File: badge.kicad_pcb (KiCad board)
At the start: 2 copper layers, 68.6 x 129.5 mm, 38 parts, among them J1 DevKitC_L, J10 IR333C, J11 DUST, J12 DevKitC_L_SMD, J13 DevKitC_R_SMD, J14 220uF, J2 DevKitC_R, J4 ADC_3, J5 ADC_2, J6 ADC_1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

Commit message: Change button
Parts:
- removed the J6 at (166.4, 116.8) (x3)
- removed the SW6 at (149.9, 109.2)
- added J6 (x3): ADC_1, custom_footprint:PinSocket_1x04_P2.54mm_Vertical_NO3D_2S, F.Cu at (166.4, 116.8)
- added SW6: B, Button_Switch_SMD:SW_SPST_PTS645, F.Cu at (152.4, 111.8)
- added SW6: B, Button_Switch_SMD:SW_SPST_PTS810, F.Cu at (149.9, 109.2)
- SW3: footprint Button_Switch_SMD:SW_SPST_TL3342 -> Button_Switch_SMD:SW_SPST_PTS645
- moved SW7 3.59 mm to (121.9, 114.3)
- moved SW3 2.54 mm to (144.8, 119.4)

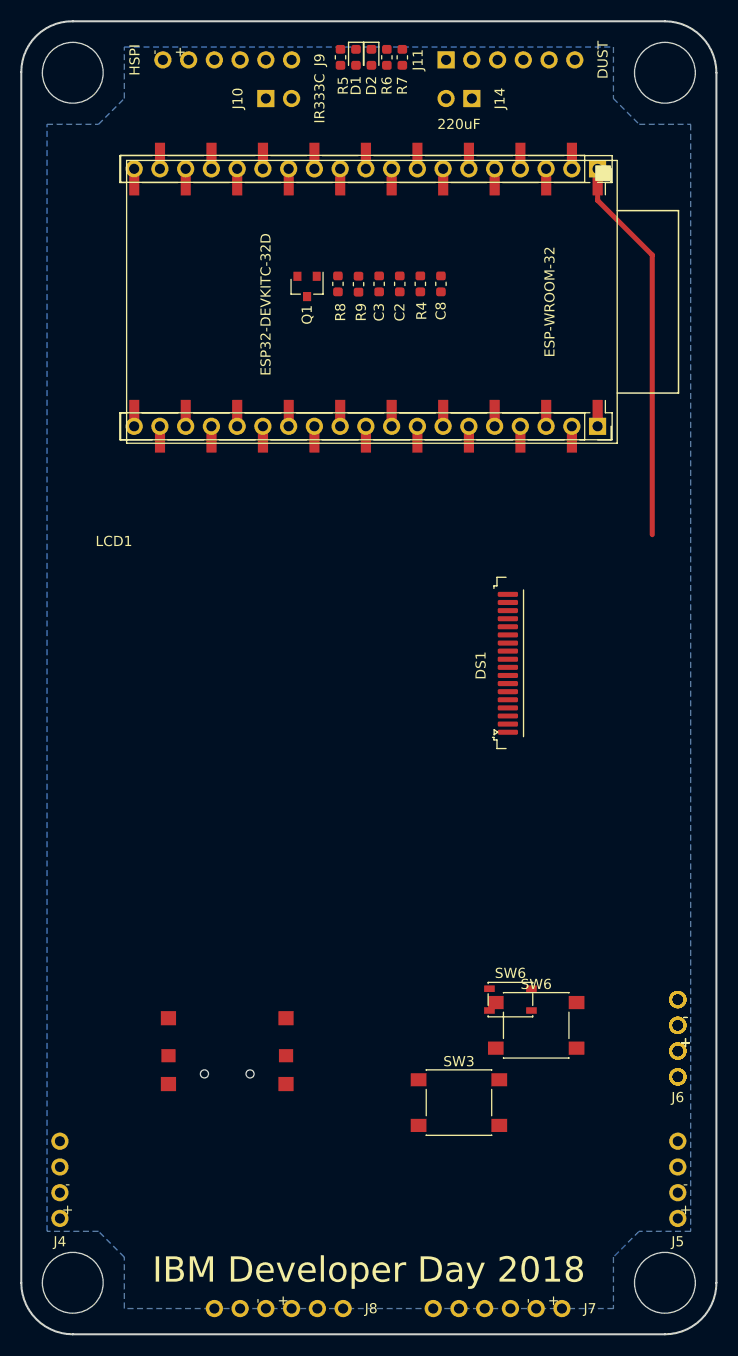
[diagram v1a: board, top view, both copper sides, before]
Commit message: Update v0.4, vertical long before tracks
* Move footprint library to DeveloperDay2018Badge
* Add symbol library, 3D models into project
* Change board color
* Increase R, C, LED size to 0805(2012)
* Remove front solder mask for ESP32 DevKitC socket header, to make clean SMD socket pad.
* Add silk for ESP32 DevKitC
* Add silk direction in footprint for ITS-1550S-B 5 way tact switch
* Add footprint and 3D for ITS-1106 tact switch
* Change ESP32 DevKitC 3D model from SnapEDA
* Remove THT 19pin socket 3D for ESP32 DevKitC
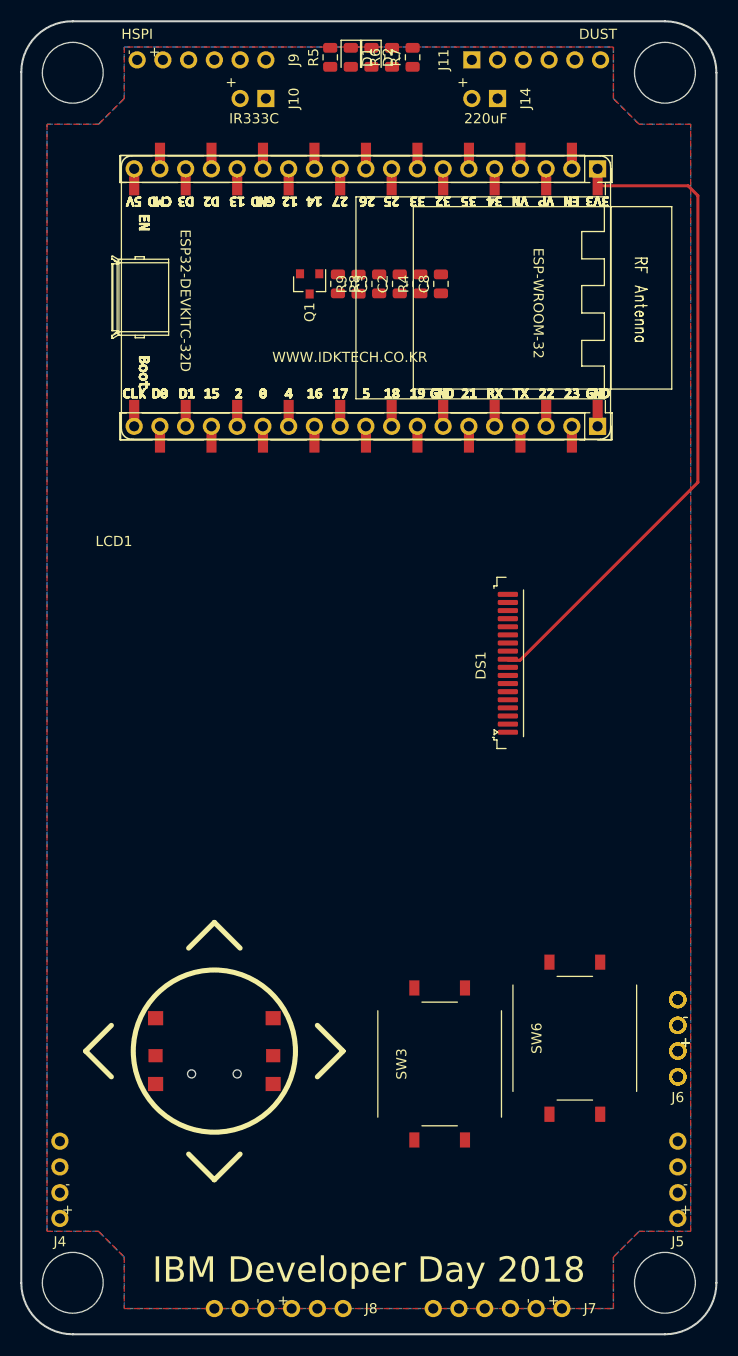
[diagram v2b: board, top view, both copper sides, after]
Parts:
- removed the J6 at (166.4, 116.8) (x3)
- removed the SW6 at (152.4, 111.8)
- removed the SW6 at (149.9, 109.2)
- added J6 (x3): ADC_1, custom_footprint:PinSocket_1x04_P2.54mm_Vertical_NO3D_2S, F.Cu at (166.4, 116.8)
- added SW6: B, DeveloperDay2018Badge:ITS-1106S, F.Cu at (156.2, 113.0)
- C2, C3: value 0603/0.1uF -> 2012/0.1uF; footprint Capacitor_SMD:C_0603_1608Metric -> Capacitor_SMD:C_0805_2012Metric
- C8: value 0.1uF -> 2012/0.1uF; footprint Capacitor_SMD:C_0603_1608Metric -> Capacitor_SMD:C_0805_2012Metric
- D1: value 0603/BLUE -> 2012/BLUE; footprint LED_SMD:LED_0603_1608Metric -> LED_SMD:LED_0805_2012Metric
- D2: value 0603/RED -> 2012/RED; footprint LED_SMD:LED_0603_1608Metric -> LED_SMD:LED_0805_2012Metric
- J1, J2: footprint Connector_PinSocket_2.54mm:PinSocket_1x19_P2.54mm_Vertical -> DeveloperDay2018Badge:PinSocket_1x19_P2.54mm_Vertical_BackOnly_NO3D
- J10, J14: footprint custom_footprint:PinSocket_1x02_P2.54mm_Vertical_NO3D -> DeveloperDay2018Badge:PinSocket_1x02_P2.54mm_Vertical_NO3D
- LCD1: footprint custom_footprint:2.4INCH_TFT_LCD_18P_0.80mm_FOLD -> DeveloperDay2018Badge:2.4INCH_TFT_LCD_18P_0.80mm_FOLD_JGKONG
- R4: value 0603/4.7R -> 2012/4.7R; footprint Resistor_SMD:R_0603_1608Metric -> Resistor_SMD:R_0805_2012Metric
- R5: value 0603/470R -> 2012/470R; footprint Resistor_SMD:R_0603_1608Metric -> Resistor_SMD:R_0805_2012Metric
- R6: value 0603/1K -> 2012/1K; footprint Resistor_SMD:R_0603_1608Metric -> Resistor_SMD:R_0805_2012Metric
- R7: value 0603/220R -> 2012/220R; footprint Resistor_SMD:R_0603_1608Metric -> Resistor_SMD:R_0805_2012Metric
- R8: value 0603/20R -> 2012/20R; footprint Resistor_SMD:R_0603_1608Metric -> Resistor_SMD:R_0805_2012Metric
- R9: value 0603/36R -> 2012/36R; footprint Resistor_SMD:R_0603_1608Metric -> Resistor_SMD:R_0805_2012Metric
- SW3: footprint Button_Switch_SMD:SW_SPST_PTS645 -> DeveloperDay2018Badge:ITS-1106S
- SW7: value SW_DIP_x03 -> ITS_1500S_B; footprint custom_footprint:ITS-1500S-A -> DeveloperDay2018Badge:ITS-1500S-B-SILKDIR
- U1: footprint custom_footprint:MODULE_ESP32-DEVKITC-32D-SILKONLY -> DeveloperDay2018Badge:MODULE_ESP32-DEVKITC-32D-SILKONLY-SIMPLE
- moved SW3 4.26 mm to (142.9, 115.6), turned to 90 degrees
- moved J11 2.54 mm to (146.1, 16.5)
- moved J9 2.54 mm to (125.7, 16.5)
- moved J14 2.54 mm to (148.6, 20.3)
- moved SW7 1.27 mm to (120.7, 114.3)
- moved R5 1.02 mm to (132.1, 16.3)
- moved R7 1.02 mm to (140.2, 16.3)
- moved U1 0.65 mm to (138.7, 40.0)
- moved D1 0.51 mm to (134.1, 16.3)
- moved R6 0.51 mm to (138.2, 16.3)
- moved Q1 0.36 mm to (130.0, 38.6)
- turned J10 to 270 degrees
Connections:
- J10 pad 2: +3V3 -> +5V
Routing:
- net +3V3: track 38.3 -> 66.3 mm
- added copper zone on F.Cu, net GND
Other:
- net class Default: trace_width 0.5 -> 0.3
- board text added: "WWW.IDKTECH.CO.KR"

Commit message: Rout'ing
* Add dummy pad for ESP32 DevKitC footprint to avoid errors
* Add silk guide for LCD attachment
* Add alternative 40pin LCD connector
* Add logo and information in silk layer
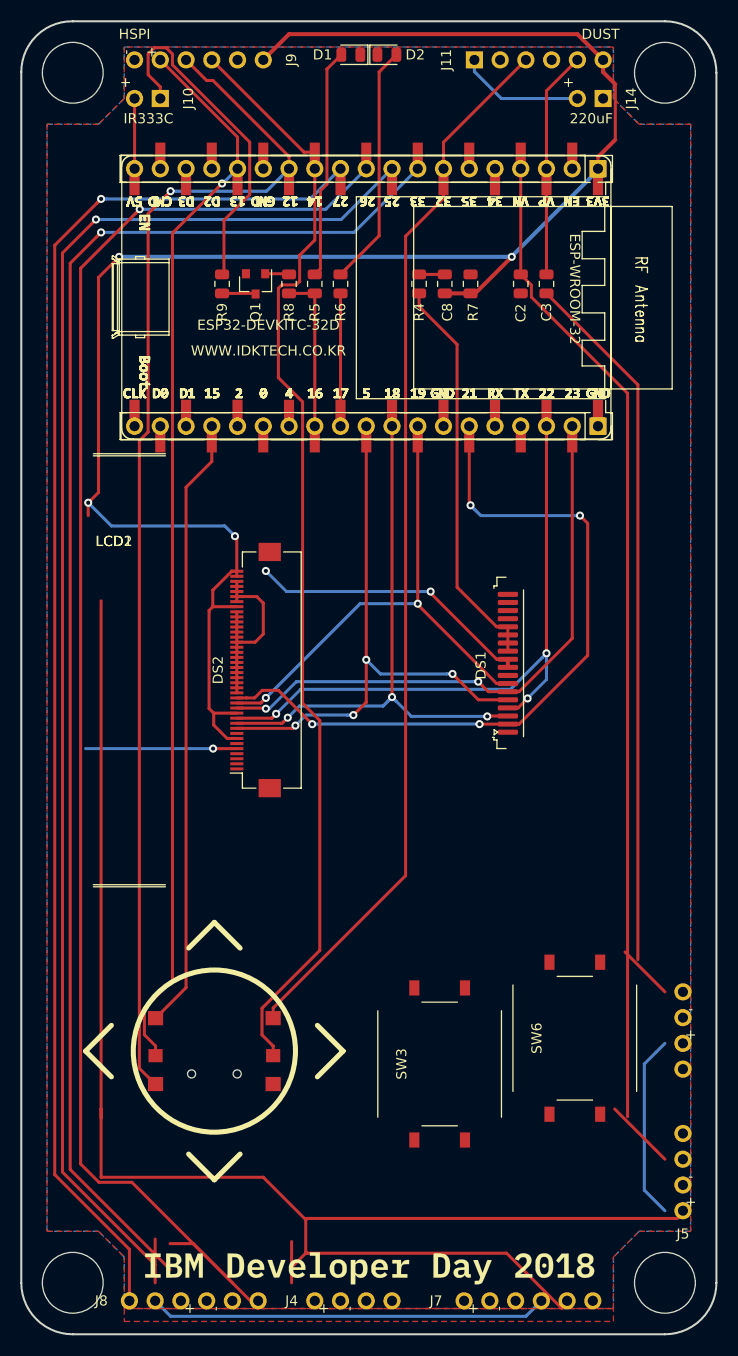
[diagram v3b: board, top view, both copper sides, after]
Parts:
- removed the J6 at (166.4, 116.8) (x4)
- added DS2: 40PIN LCD, Connector_FFC-FPC:Hirose_FH12-40S-0.5SH_1x40-1MP_P0.50mm_Horizontal, F.Cu at (124.7, 76.7)
- added G***: LOGO, LOGO, B.Cu at (121.9, 129.5)
- added G***: LOGO, LOGO, B.Cu at (135.9, 114.3)
- added G***: Badge URL, LOGO, B.Cu at (143.5, 62.2)
- added G***: LOGO_INFO, LOGO, B.Cu at (142.2, 95.2)
- added G***: Front Logo, DeveloperDay2018Badge:LOGO_Front, F.Cu at (136.4, 135.6)
- added G***: LOGO, LOGO, B.Cu at (149.9, 77.5)
- added J6: ADC_1, custom_footprint:PinSocket_1x04_P2.54mm_Vertical_NO3D_2S, F.Cu at (166.9, 116.1)
- added LCD2: 2.4" LCD 40PIN, DeveloperDay2018Badge:2.4INCH_TFT_LCD_40P_0.50mm_FOLD, F.Cu at (105.7, 55.4)
- DS1: value EZ240IT010 -> 18PIN LCD
- LCD1: value 2.4" LCD -> 2.4" LCD 18PIN
- moved J4 26.4 mm to (130.6, 138.9), turned to 90 degrees
- moved R7 23.1 mm to (145.9, 38.6), turned to 270 degrees
- moved R6 22.9 mm to (133.1, 38.6), turned to 270 degrees
- moved R5 22.4 mm to (130.6, 38.6), turned to 270 degrees
- moved J8 21.1 mm to (112.3, 138.9), turned to 90 degrees
- moved C3 16.5 mm to (153.4, 38.6)
- moved R9 13.5 mm to (121.4, 38.6)
- moved C2 11.9 mm to (150.9, 38.6)
- moved J10 10.4 mm to (115.3, 20.3)
- moved J14 10.4 mm to (159.0, 20.3)
- moved J7 9.68 mm to (145.3, 138.9), turned to 90 degrees
- moved Q1 5.33 mm to (124.7, 38.6)
- moved R8 4.83 mm to (128.0, 38.6)
- moved D2 1.55 mm to (137.7, 16.0), turned to 0 degrees
- moved J5 0.92 mm to (166.9, 130.0)
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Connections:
- C2 pad 2: /GPIO36 -> /GPIO39
- C3 pad 2: /GPIO39 -> /GPIO36
- D1 pad 1: Net-(D1-Pad1) -> GND
- D1 pad 2: /GPIO16 -> Net-(D1-Pad2)
- D2 pad 1: Net-(D2-Pad1) -> GND
- D2 pad 2: /GPIO17 -> Net-(D2-Pad2)
- J5 pad 3: /GPIO36 -> /GPIO39
- J5 pad 4: /GPIO39 -> /GPIO36
- R5 pad 1: GND -> Net-(D1-Pad2)
- R5 pad 2: Net-(D1-Pad1) -> /GPIO16
- R6 pad 1: GND -> Net-(D2-Pad2)
- R6 pad 2: Net-(D2-Pad1) -> /GPIO17
- R8 pad 2: /GPIO27 -> /GPIO16
- SW7 pad 1: /GPIO12 -> /GPIO15
- SW7 pad 3: /GPIO14 -> /GPIO12
- SW7 pad 5: /GPIO15 -> /GPIO14
- SW7 pad 6: /GPIO39 -> /GPIO32
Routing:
- net /GPIO33: track 1.63 -> 296.5 mm, vias 0 -> 1
- net /GPIO25: track 1.68 -> 184.9 mm, vias 0 -> 1
- net +3V3: track 66.3 -> 224.2 mm, vias 0 -> 6
- net /GPIO26: track 1.63 -> 153.4 mm, vias 0 -> 1
- net /GPIO27: track 1.68 -> 140.9 mm, vias 0 -> 1
- net /GPIO12: track 1.68 -> 119.6 mm, vias 0 -> 1
- net /GPIO14: track 1.63 -> 109.9 mm
- net /GPIO13: track 1.68 -> 107.4 mm, vias 0 -> 1
- net /GPIO39: track 1.63 -> 106.5 mm
- net /GPIO32: track 1.68 -> 103.2 mm
- net Net-(C3-Pad1): track 0.00 -> 75.0 mm
- net /LCD_RST: track 1.65 -> 72.3 mm, vias 0 -> 4
- net /LCD_DC: track 1.66 -> 64.8 mm, vias 0 -> 3
- net /GPIO15: track 1.65 -> 60.7 mm
- net /VSPI_MOSI: track 1.65 -> 57.8 mm, vias 0 -> 2
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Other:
- net class Default: clearance 0.5 -> 0.2
- net class Touch trace: clearance 0.5 -> 0.3
- net class VCC added: clearance 0.3, trace_width 0.4, via_dia 0.8, via_drill 0.4
- rule trace_clearance: 0.5 -> 0.2
- board text removed: "IBM Developer Day 2018"

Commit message: v0.5 Finish tracks, final review
* Remove paste at 18pin LCD
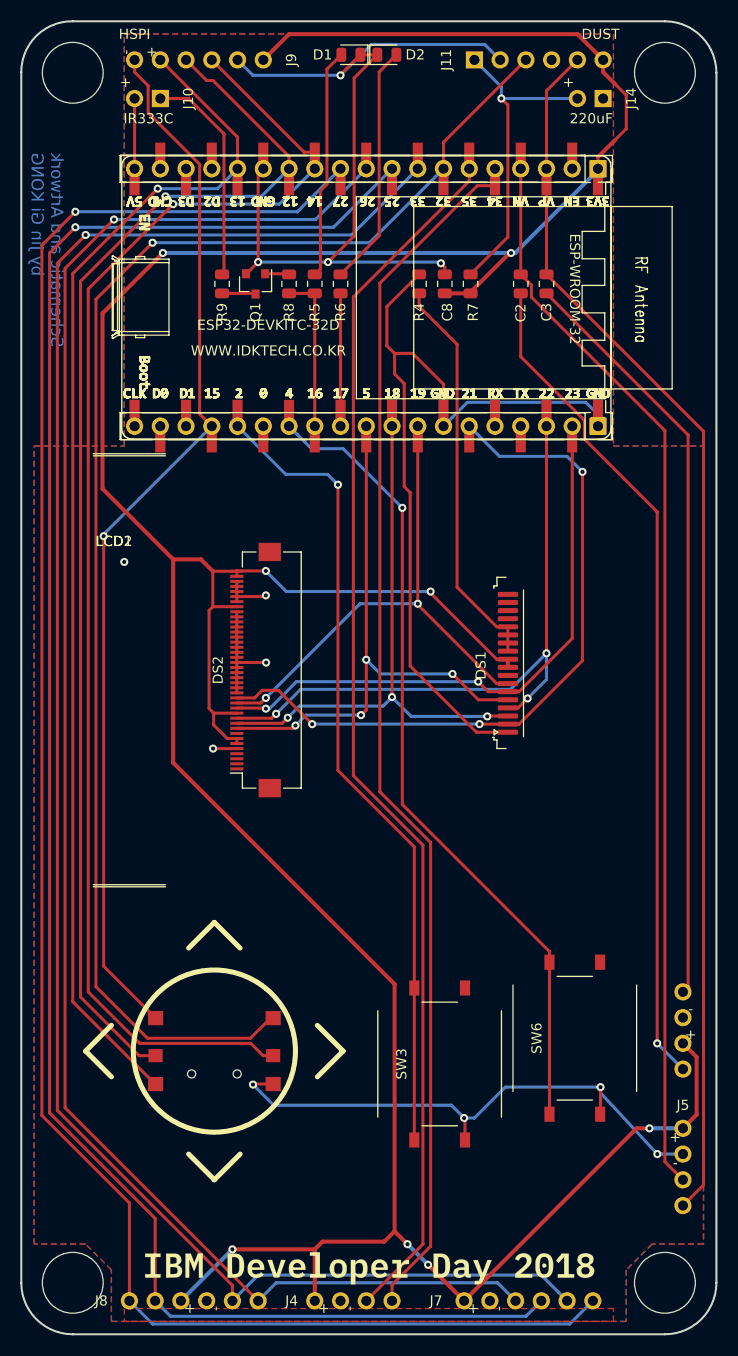
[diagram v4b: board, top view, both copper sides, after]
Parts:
- removed the G*** at (135.9, 114.3)
- added G***: LOGO CREDIT, DeveloperDay2018Badge:LOGO_CREDIT, B.Cu at (137.2, 113.0)
- DS1: footprint custom_footprint:COMMON_MOUNT_FFC-1x18-1MP_P0.80mm -> DeveloperDay2018Badge:COMMON_MOUNT_FFC-1x18-1MP_P0.80mm
- moved G*** 35.6 mm to (142.2, 59.7)
- moved G*** 30.5 mm to (143.5, 92.7)
- moved J5 8.13 mm to (166.9, 121.9), turned to 0 degrees
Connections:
- J4 pad 3: /GPIO34 -> /GPIO35
- J4 pad 4: /GPIO35 -> /GPIO34
- SW3 pad 1: /GPIO4 -> /GPIO2
- SW6 pad 1: /GPIO2 -> /GPIO4
- SW7 pad 2: /GPIO13 -> /GPIO12
- SW7 pad 3: /GPIO12 -> /GPIO13
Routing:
- net GND: track 36.3 -> 244.4 mm, vias 1 -> 12
- net +3V3: track 224.2 -> 354.6 mm, vias 6 -> 8
- net /GPIO35: track 1.63 -> 123.2 mm
- net /GPIO34: track 1.67 -> 121.1 mm
- net /GPIO33: track 296.5 -> 185.7 mm
- net /GPIO36: track 22.4 -> 121.6 mm
- net Net-(C2-Pad1): track 0.00 -> 83.2 mm, vias 0 -> 1
- net /GPIO4: track 1.65 -> 82.0 mm, vias 0 -> 1
- net /GPIO2: track 1.65 -> 81.7 mm, vias 0 -> 1
- net /GPIO27: track 140.9 -> 190.4 mm
- net /GPIO15: track 60.7 -> 106.2 mm, vias 0 -> 1
- net /GPIO32: track 103.2 -> 143.6 mm, vias 0 -> 1
- net /GPIO14: track 109.9 -> 133.0 mm, vias 0 -> 1
- net Net-(J11-Pad1): track 12.4 -> 31.6 mm, vias 0 -> 1
- net /GPIO26: track 153.4 -> 172.0 mm
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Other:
- board text added: "Schematic and Artwork by Jin Gi KONG"

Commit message: v1.0 release
* Update 40pin footprint
* Update tracks
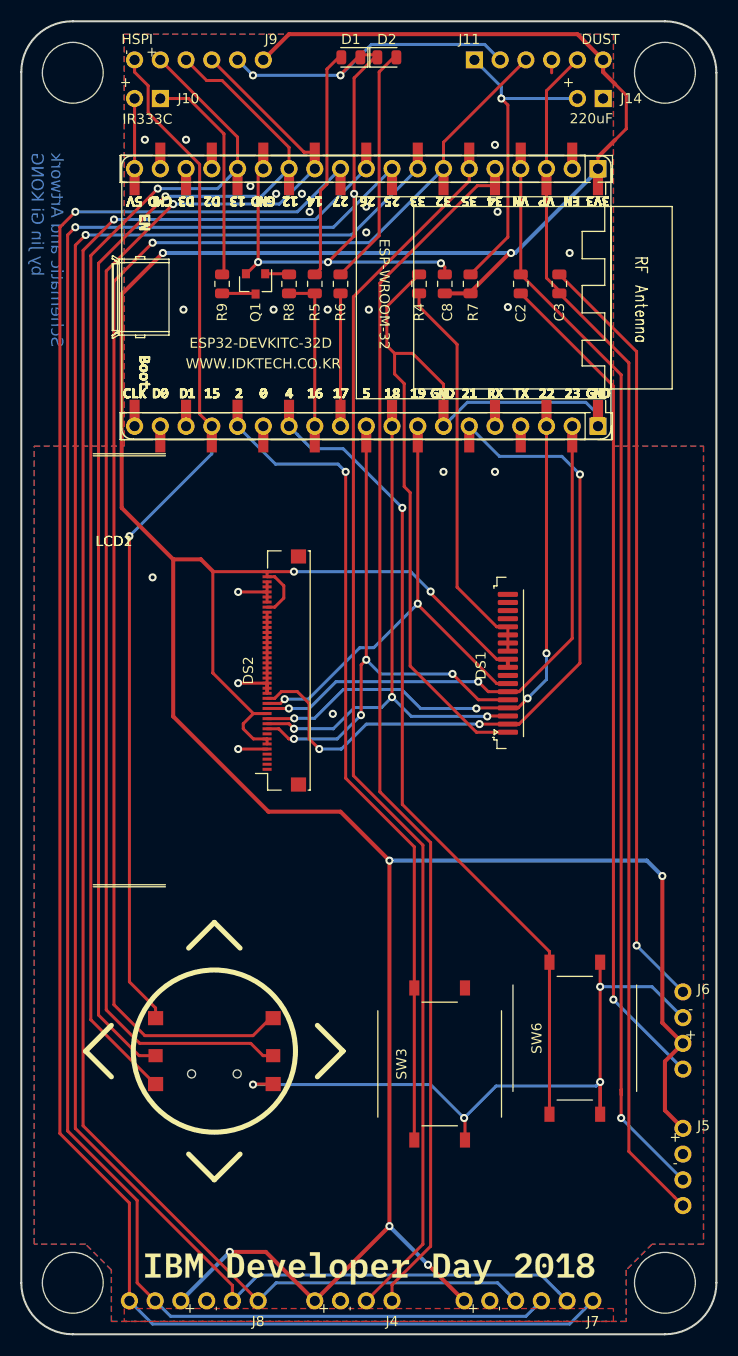
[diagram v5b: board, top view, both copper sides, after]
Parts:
- DS2: footprint Connector_FFC-FPC:Hirose_FH12-40S-0.5SH_1x40-1MP_P0.50mm_Horizontal -> DeveloperDay2018Badge:Yeonho_05002HR-40C_1x40-1MP_P0.50mm_Horizontal
- moved G*** 36.1 mm to (142.2, 95.8)
- moved G*** 4.85 mm to (149.4, 72.6)
- moved G*** 4.85 mm to (143.0, 87.9)
- moved DS2 2.99 mm to (127.7, 76.8)
- moved C3 1.27 mm to (154.7, 38.6), turned to 270 degrees
- moved G*** 1.27 mm to (137.2, 111.8)
- moved D1 0.25 mm to (134.1, 16.3)
- moved D2 0.25 mm to (137.7, 16.3)
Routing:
- net +3V3: track 354.6 -> 376.3 mm, vias 8 -> 9
- net GND: track 244.4 -> 260.4 mm, vias 12 -> 33
- net /LCD_DC: track 64.8 -> 57.4 mm, vias 3 -> 4
- net /VSPI_MOSI: track 57.8 -> 54.7 mm
- net /VSPI_MISO: track 51.6 -> 48.7 mm
- net /VSPI_SCK: track 57.0 -> 54.4 mm
- net /GPIO15: track 106.2 -> 103.8 mm
- net /VSPI_CS: track 57.1 -> 55.0 mm
- net /GPIO32: track 143.6 -> 141.9 mm
- net /GPIO36: track 121.6 -> 120.0 mm
- net /GPIO14: track 133.0 -> 131.6 mm
- net /GPIO27: track 190.4 -> 188.9 mm
- net /GPIO26: track 172.0 -> 170.6 mm
- net /GPIO25: track 186.0 -> 184.5 mm
- net /GPIO13: track 119.5 -> 118.0 mm
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
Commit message: Fix 3D model path into project
* Change R values
* Fix a few tracks
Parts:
- removed J12: DevKitC_L_SMD, Connector_PinSocket_2.54mm:PinSocket_1x19_P2.54mm_Vertical_SMD_Pin1Right
- H1, H2, H5, H6: footprint custom_footprint:LanyardHole_6mm -> DeveloperDay2018Badge:LanyardHole_6mm
- J1: footprint DeveloperDay2018Badge:PinSocket_1x19_P2.54mm_Vertical_BackOnly_NO3D -> DeveloperDay2018Badge:PinSocket_1x19_P2.54mm_Vertical_Universal_Pin1Right
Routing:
- net /GPIO12: track 121.6 -> 120.0 mm
- net /GPIO15: track 103.8 -> 105.4 mm
- net +3V3: track 376.3 -> 377.8 mm
- net /GPIO32: track 141.9 -> 142.2 mm, vias 1 -> 2
- net GND: vias 33 -> 32
